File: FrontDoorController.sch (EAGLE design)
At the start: 10 parts

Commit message: Door_Control_PCB: Add Particle Logo
Add the Particle (Spark) logo to the board to make it cooler looking and
more official (not at all official).
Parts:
- added U$1: SPARK_LOGOLARGE, Mikes-Stuff:SPARK_LOGOLARGE
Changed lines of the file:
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@@
 <grid distance="0.1" unitdist="inch" unit="inch" style="lines" multiple="1" display="no" altdistance="0.01" altunitdist="inch" altunit="inch"/>
 <layers>
-<layer number="1" name="Top" color="4" fill="1" visible="no" active="no"/>
-<layer number="16" name="Bottom" color="1" fill="1" visible="no" active="no"/>
-<layer number="17" name="Pads" color="2" fill="1" visible="no" active="no"/>
-<layer number="18" name="Vias" color="2" fill="1" visible="no" active="no"/>
-<layer number="19" name="Unrouted" color="6" fill="1" visible="no" active="no"/>
-<layer number="20" name="Dimension" color="15" fill="1" visible="no" active="no"/>
-<layer number="21" name="tPlace" color="16" fill="1" visible="no" active="no"/>
-<layer number="22" name="bPlace" color="7" fill="1" visible="no" active="no"/>
-<layer number="23" name="tOrigins" color="15" fill="1" visible="no" active="no"/>
-<layer number="24" name="bOrigins" color="15" fill="1" visible="no" active="no"/>
-<layer number="25" name="tNames" color="7" fill="1" visible="no" active="no"/>
-<layer number="26" name="bNames" color="7" fill="1" visible="no" active="no"/>
-<layer number="27" name="tValues" color="7" fill="1" visible="no" active="no"/>
-<layer number="28" name="bValues" color="7" fill="1" visible="no" active="no"/>
+<layer number="1" name="Top" color="4" fill="1" visible="yes" active="no"/>
+<layer number="16" name="Bottom" color="1" fill="1" visible="yes" active="no"/>
+<layer number="17" name="Pads" color="2" fill="1" visible="yes" active="no"/>
+<layer number="18" name="Vias" color="2" fill="1" visible="yes" active="no"/>
+<layer number="19" name="Unrouted" color="6" fill="1" visible="yes" active="no"/>
+<layer number="20" name="Dimension" color="15" fill="1" visible="yes" active="no"/>
+<layer number="21" name="tPlace" color="7" fill="1" visible="yes" active="no"/>
+<layer number="22" name="bPlace" color="7" fill="1" visible="yes" active="no"/>
+<layer number="23" name="tOrigins" color="15" fill="1" visible="yes" active="no"/>
+<layer number="24" name="bOrigins" color="15" fill="1" visible="yes" active="no"/>
+<layer number="25" name="tNames" color="7" fill="1" visible="yes" active="no"/>
+<layer number="26" name="bNames" color="7" fill="1" visible="yes" active="no"/>
+<layer number="27" name="tValues" color="7" fill="1" visible="yes" active="no"/>
+<layer number="28" name="bValues" color="7" fill="1" visible="yes" active="no"/>
 <layer number="29" name="tStop" color="7" fill="3" visible="no" active="no"/>
 <layer number="30" name="bStop" color="7" fill="6" visible="no" active="no"/>
@@
 <layer number="35" name="tGlue" color="7" fill="4" visible="no" active="no"/>
 <layer number="36" name="bGlue" color="7" fill="5" visible="no" active="no"/>
-<layer number="37" name="tTest" color="7" fill="1" visible="no" active="no"/>
-<layer number="38" name="bTest" color="7" fill="1" visible="no" active="no"/>
+<layer number="37" name="tTest" color="7" fill="1" visible="yes" active="no"/>
+<layer number="38" name="bTest" color="7" fill="1" visible="yes" active="no"/>
 <layer number="39" name="tKeepout" color="4" fill="11" visible="no" active="no"/>
 <layer number="40" name="bKeepout" color="1" fill="11" visible="no" active="no"/>
@@
 <layer number="44" name="Drills" color="7" fill="1" visible="no" active="no"/>
 <layer number="45" name="Holes" color="7" fill="1" visible="no" active="no"/>
-<layer number="46" name="Milling" color="3" fill="1" visible="no" active="no"/>
-<layer number="47" name="Measures" color="7" fill="1" visible="no" active="no"/>
-<layer number="48" name="Document" color="7" fill="1" visible="no" active="no"/>
-<layer number="49" name="Reference" color="7" fill="1" visible="no" active="no"/>
-<layer number="50" name="dxf" color="7" fill="1" visible="no" active="no"/>
-<layer number="51" name="tDocu" color="14" fill="1" visible="no" active="no"/>
-<layer number="52" name="bDocu" color="7" fill="1" visible="no" active="no"/>
-<layer number="53" name="tGND_GNDA" color="7" fill="9" visible="no" active="no"/>
-<layer number="54" name="bGND_GNDA" color="1" fill="9" visible="no" active="no"/>
-<layer number="56" name="wert" color="7" fill="1" visible="no" active="no"/>
-<layer number="57" name="tCAD" color="7" fill="1" visible="no" active="no"/>
-<layer number="59" name="tCarbon" color="7" fill="1" visible="no" active="no"/>
-<layer number="60" name="bCarbon" color="7" fill="1" visible="no" active="no"/>
+<layer number="46" name="Milling" color="3" fill="1" visible="yes" active="no"/>
+<layer number="47" name="Measures" color="7" fill="1" visible="yes" active="no"/>
+<layer number="48" name="Document" color="7" fill="1" visible="yes" active="no"/>
+<layer number="49" name="Reference" color="7" fill="1" visible="yes" active="no"/>
+<layer number="50" name="dxf" color="7" fill="1" visible="yes" active="no"/>
+<layer number="51" name="tDocu" color="7" fill="1" visible="yes" active="no"/>
+<layer number="52" name="bDocu" color="7" fill="1" visible="yes" active="no"/>
+<layer number="53" name="tGND_GNDA" color="7" fill="9" visible="yes" active="no"/>
+<layer number="54" name="bGND_GNDA" color="1" fill="9" visible="yes" active="no"/>
+<layer number="56" name="wert" color="7" fill="1" visible="yes" active="no"/>
+<layer number="57" name="tCAD" color="7" fill="1" visible="yes" active="no"/>
+<layer number="59" name="tCarbon" color="7" fill="1" visible="yes" active="no"/>
+<layer number="60" name="bCarbon" color="7" fill="1" visible="yes" active="no"/>
 <layer number="90" name="Modules" color="5" fill="1" visible="no" active="no"/>
 <layer number="91" name="Nets" color="2" fill="1" visible="yes" active="yes"/>
@@
 <part name="U$3" library="Spark" deviceset="PHOTON" device="_WITH_HEADERS"/>
 <part name="R1" library="SparkFun-Resistors" deviceset="RESISTOR" device="0603" value="1K"/>
+<part name="U$1" library="Mikes-Stuff" deviceset="SPARK_LOGO" device="LARGE"/>
 </parts>
 <sheets>
@@
 <instance part="U$3" gate="G$1" x="30.48" y="81.153"/>
 <instance part="R1" gate="G$1" x="119.38" y="127"/>
+<instance part="U$1" gate="G$1" x="15.24" y="38.1"/>
 </instances>
 <busses>

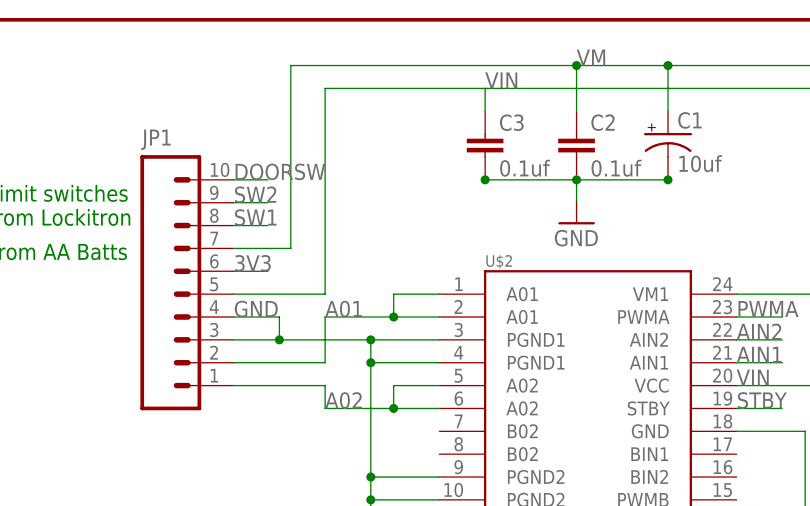
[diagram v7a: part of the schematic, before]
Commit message: Door_Control_PCB: Add locking Photon and reroute
Add the locking Photon from Mike's Library so that I can try out the
connections before soldering.  Also reroute some things and make a few
traces bigger and move some of the header pins around.
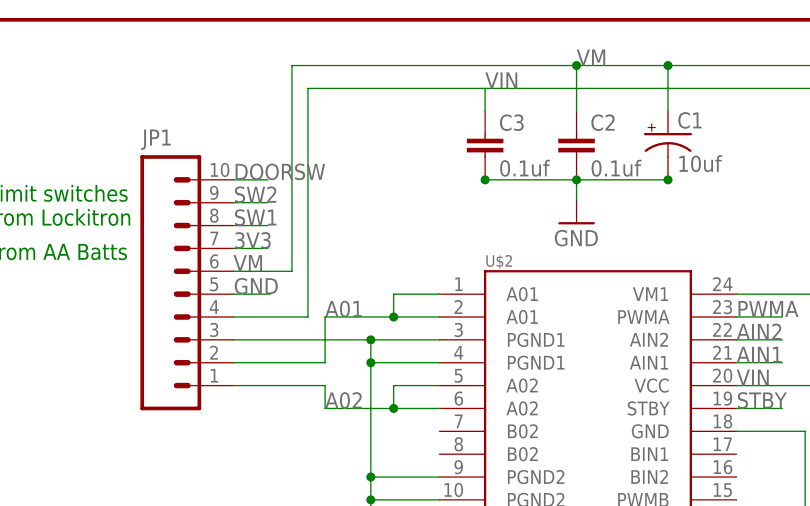
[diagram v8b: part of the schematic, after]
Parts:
- U$3: device Spark:PHOTON_WITH_HEADERS -> Mikes-Stuff:PHOTON_WITH_HEADERS
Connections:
- net 3V3: now also JP1.7; no longer JP1.6
- net GND: now also JP1.5; no longer JP1.4
- net VIN: now also JP1.4; no longer JP1.5
- net VM: now also JP1.6; no longer JP1.7
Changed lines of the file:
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@@
 <setting verticaltext="up"/>
 </settings>
-<grid distance="0.1" unitdist="inch" unit="inch" style="lines" multiple="1" display="no" altdistance="0.01" altunitdist="inch" altunit="inch"/>
+<grid distance="0.05" unitdist="inch" unit="inch" style="lines" multiple="1" display="no" altdistance="0.001" altunitdist="inch" altunit="inch"/>
 <layers>
-<layer number="1" name="Top" color="4" fill="1" visible="yes" active="no"/>
-<layer number="16" name="Bottom" color="1" fill="1" visible="yes" active="no"/>
-<layer number="17" name="Pads" color="2" fill="1" visible="yes" active="no"/>
-<layer number="18" name="Vias" color="2" fill="1" visible="yes" active="no"/>
-<layer number="19" name="Unrouted" color="6" fill="1" visible="yes" active="no"/>
-<layer number="20" name="Dimension" color="15" fill="1" visible="yes" active="no"/>
-<layer number="21" name="tPlace" color="7" fill="1" visible="yes" active="no"/>
-<layer number="22" name="bPlace" color="7" fill="1" visible="yes" active="no"/>
-<layer number="23" name="tOrigins" color="15" fill="1" visible="yes" active="no"/>
-<layer number="24" name="bOrigins" color="15" fill="1" visible="yes" active="no"/>
-<layer number="25" name="tNames" color="7" fill="1" visible="yes" active="no"/>
-<layer number="26" name="bNames" color="7" fill="1" visible="yes" active="no"/>
-<layer number="27" name="tValues" color="7" fill="1" visible="yes" active="no"/>
-<layer number="28" name="bValues" color="7" fill="1" visible="yes" active="no"/>
+<layer number="1" name="Top" color="4" fill="1" visible="no" active="no"/>
+<layer number="16" name="Bottom" color="1" fill="1" visible="no" active="no"/>
+<layer number="17" name="Pads" color="2" fill="1" visible="no" active="no"/>
+<layer number="18" name="Vias" color="2" fill="1" visible="no" active="no"/>
+<layer number="19" name="Unrouted" color="6" fill="1" visible="no" active="no"/>
+<layer number="20" name="Dimension" color="15" fill="1" visible="no" active="no"/>
+<layer number="21" name="tPlace" color="7" fill="1" visible="no" active="no"/>
+<layer number="22" name="bPlace" color="7" fill="1" visible="no" active="no"/>
+<layer number="23" name="tOrigins" color="15" fill="1" visible="no" active="no"/>
+<layer number="24" name="bOrigins" color="15" fill="1" visible="no" active="no"/>
+<layer number="25" name="tNames" color="7" fill="1" visible="no" active="no"/>
+<layer number="26" name="bNames" color="7" fill="1" visible="no" active="no"/>
+<layer number="27" name="tValues" color="7" fill="1" visible="no" active="no"/>
+<layer number="28" name="bValues" color="7" fill="1" visible="no" active="no"/>
 <layer number="29" name="tStop" color="7" fill="3" visible="no" active="no"/>
 <layer number="30" name="bStop" color="7" fill="6" visible="no" active="no"/>
@@
 <layer number="35" name="tGlue" color="7" fill="4" visible="no" active="no"/>
 <layer number="36" name="bGlue" color="7" fill="5" visible="no" active="no"/>
-<layer number="37" name="tTest" color="7" fill="1" visible="yes" active="no"/>
-<layer number="38" name="bTest" color="7" fill="1" visible="yes" active="no"/>
+<layer number="37" name="tTest" color="7" fill="1" visible="no" active="no"/>
+<layer number="38" name="bTest" color="7" fill="1" visible="no" active="no"/>
 <layer number="39" name="tKeepout" color="4" fill="11" visible="no" active="no"/>
 <layer number="40" name="bKeepout" color="1" fill="11" visible="no" active="no"/>
@@
 <layer number="44" name="Drills" color="7" fill="1" visible="no" active="no"/>
 <layer number="45" name="Holes" color="7" fill="1" visible="no" active="no"/>
-<layer number="46" name="Milling" color="3" fill="1" visible="yes" active="no"/>
-<layer number="47" name="Measures" color="7" fill="1" visible="yes" active="no"/>
-<layer number="48" name="Document" color="7" fill="1" visible="yes" active="no"/>
-<layer number="49" name="Reference" color="7" fill="1" visible="yes" active="no"/>
-<layer number="50" name="dxf" color="7" fill="1" visible="yes" active="no"/>
-<layer number="51" name="tDocu" color="7" fill="1" visible="yes" active="no"/>
-<layer number="52" name="bDocu" color="7" fill="1" visible="yes" active="no"/>
-<layer number="53" name="tGND_GNDA" color="7" fill="9" visible="yes" active="no"/>
-<layer number="54" name="bGND_GNDA" color="1" fill="9" visible="yes" active="no"/>
-<layer number="56" name="wert" color="7" fill="1" visible="yes" active="no"/>
-<layer number="57" name="tCAD" color="7" fill="1" visible="yes" active="no"/>
-<layer number="59" name="tCarbon" color="7" fill="1" visible="yes" active="no"/>
-<layer number="60" name="bCarbon" color="7" fill="1" visible="yes" active="no"/>
+<layer number="46" name="Milling" color="3" fill="1" visible="no" active="no"/>
+<layer number="47" name="Measures" color="7" fill="1" visible="no" active="no"/>
+<layer number="48" name="Document" color="7" fill="1" visible="no" active="no"/>
+<layer number="49" name="Reference" color="7" fill="1" visible="no" active="no"/>
+<layer number="50" name="dxf" color="7" fill="1" visible="no" active="no"/>
+<layer number="51" name="tDocu" color="7" fill="1" visible="no" active="no"/>
+<layer number="52" name="bDocu" color="7" fill="1" visible="no" active="no"/>
+<layer number="53" name="tGND_GNDA" color="7" fill="9" visible="no" active="no"/>
+<layer number="54" name="bGND_GNDA" color="1" fill="9" visible="no" active="no"/>
+<layer number="56" name="wert" color="7" fill="1" visible="no" active="no"/>
+<layer number="57" name="tCAD" color="7" fill="1" visible="no" active="no"/>
+<layer number="59" name="tCarbon" color="7" fill="1" visible="no" active="no"/>
+<layer number="60" name="bCarbon" color="7" fill="1" visible="no" active="no"/>
 <layer number="90" name="Modules" color="5" fill="1" visible="no" active="no"/>
 <layer number="91" name="Nets" color="2" fill="1" visible="yes" active="yes"/>
@@
 <part name="JP1" library="SparkFun-Connectors" deviceset="M10" device="LOCK"/>
 <part name="D1" library="SparkFun-DiscreteSemi" deviceset="DIODE" device="PTH"/>
-<part name="U$3" library="Spark" deviceset="PHOTON" device="_WITH_HEADERS"/>
+<part name="U$3" library="Mikes-Stuff" deviceset="PHOTON" device="_WITH_HEADERS"/>
 <part name="R1" library="SparkFun-Resistors" deviceset="RESISTOR" device="0603" value="1K"/>
 <part name="U$1" library="Mikes-Stuff" deviceset="SPARK_LOGO" device="LARGE"/>
@@
 <label x="226.695" y="144.78" size="1.778" layer="95"/>
 <label x="198.755" y="177.8" size="1.778" layer="95"/>
-<wire x1="198.755" y1="177.8" x2="180.975" y2="177.8" width="0.1524" layer="91"/>
-<wire x1="180.975" y1="177.8" x2="180.975" y2="154.94" width="0.1524" layer="91"/>
-<pinref part="JP1" gate="G$1" pin="5"/>
-<wire x1="180.975" y1="154.94" x2="170.815" y2="154.94" width="0.1524" layer="91"/>
+<wire x1="198.755" y1="177.8" x2="179.07" y2="177.8" width="0.1524" layer="91"/>
+<pinref part="JP1" gate="G$1" pin="4"/>
+<wire x1="170.815" y1="152.4" x2="179.07" y2="152.4" width="0.1524" layer="91"/>
+<wire x1="179.07" y1="177.8" x2="179.07" y2="152.4" width="0.1524" layer="91"/>
 </segment>
 <segment>
@@
 </segment>
 <segment>
-<pinref part="JP1" gate="G$1" pin="4"/>
-<wire x1="170.815" y1="152.4" x2="175.895" y2="152.4" width="0.1524" layer="91"/>
-<label x="170.815" y="152.4" size="1.778" layer="95"/>
 <pinref part="JP1" gate="G$1" pin="3"/>
-<wire x1="170.815" y1="149.86" x2="175.895" y2="149.86" width="0.1524" layer="91"/>
-<wire x1="175.895" y1="152.4" x2="175.895" y2="149.86" width="0.1524" layer="91"/>
 <pinref part="U$2" gate="G$1" pin="GND"/>
 <wire x1="226.695" y1="139.7" x2="234.315" y2="139.7" width="0.1524" layer="91"/>
@@
 <junction x="186.055" y="134.62"/>
 <junction x="186.055" y="147.32"/>
-<wire x1="175.895" y1="149.86" x2="186.055" y2="149.86" width="0.1524" layer="91"/>
+<wire x1="170.815" y1="149.86" x2="186.055" y2="149.86" width="0.1524" layer="91"/>
 <junction x="186.055" y="149.86"/>
-<junction x="175.895" y="149.86"/>
 </segment>
 <segment>
@@
 <label x="110.236" y="127" size="1.778" layer="95"/>
 </segment>
+<segment>
+<pinref part="JP1" gate="G$1" pin="5"/>
+<wire x1="170.815" y1="154.94" x2="174.8536" y2="154.94" width="0.1524" layer="91"/>
+<label x="170.815" y="154.94" size="1.778" layer="95"/>
+</segment>
 </net>
 <net name="TX" class="0">
@@
 </segment>
 <segment>
-<pinref part="JP1" gate="G$1" pin="6"/>
-<wire x1="170.815" y1="157.48" x2="174.625" y2="157.48" width="0.1524" layer="91"/>
-<label x="170.815" y="157.48" size="1.778" layer="95"/>
+<pinref part="JP1" gate="G$1" pin="7"/>
+<wire x1="170.815" y1="160.02" x2="174.625" y2="160.02" width="0.1524" layer="91"/>
+<label x="170.815" y="160.02" size="1.778" layer="95"/>
 </segment>
 </net>
@@
 <pinref part="C2" gate="G$1" pin="1"/>
 <wire x1="208.915" y1="180.34" x2="208.915" y2="175.26" width="0.1524" layer="91"/>
-<wire x1="208.915" y1="180.34" x2="177.165" y2="180.34" width="0.1524" layer="91"/>
+<wire x1="208.915" y1="180.34" x2="177.292" y2="180.34" width="0.1524" layer="91"/>
 <junction x="219.075" y="180.34"/>
 <junction x="208.915" y="180.34"/>
-<pinref part="JP1" gate="G$1" pin="7"/>
-<wire x1="170.815" y1="160.02" x2="177.165" y2="160.02" width="0.1524" layer="91"/>
-<wire x1="177.165" y1="160.02" x2="177.165" y2="180.34" width="0.1524" layer="91"/>
-</segment>
-<segment>
+<wire x1="177.292" y1="157.48" x2="177.292" y2="180.34" width="0.1524" layer="91"/>
+<pinref part="JP1" gate="G$1" pin="6"/>
+<wire x1="170.815" y1="157.48" x2="177.292" y2="157.48" width="0.1524" layer="91"/>
+<label x="170.7896" y="157.5054" size="1.778" layer="95"/>
+</segment>
+<segment>
